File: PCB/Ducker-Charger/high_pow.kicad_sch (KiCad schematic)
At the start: 37 parts, among them Q1 NCE3080K, Q2 NCE3080K, Q3 NCE3080K, Q4 NCE3080K, Q5 NCE3080K, U1 BQ25713RSNR, U2 TPS25750DRJKR

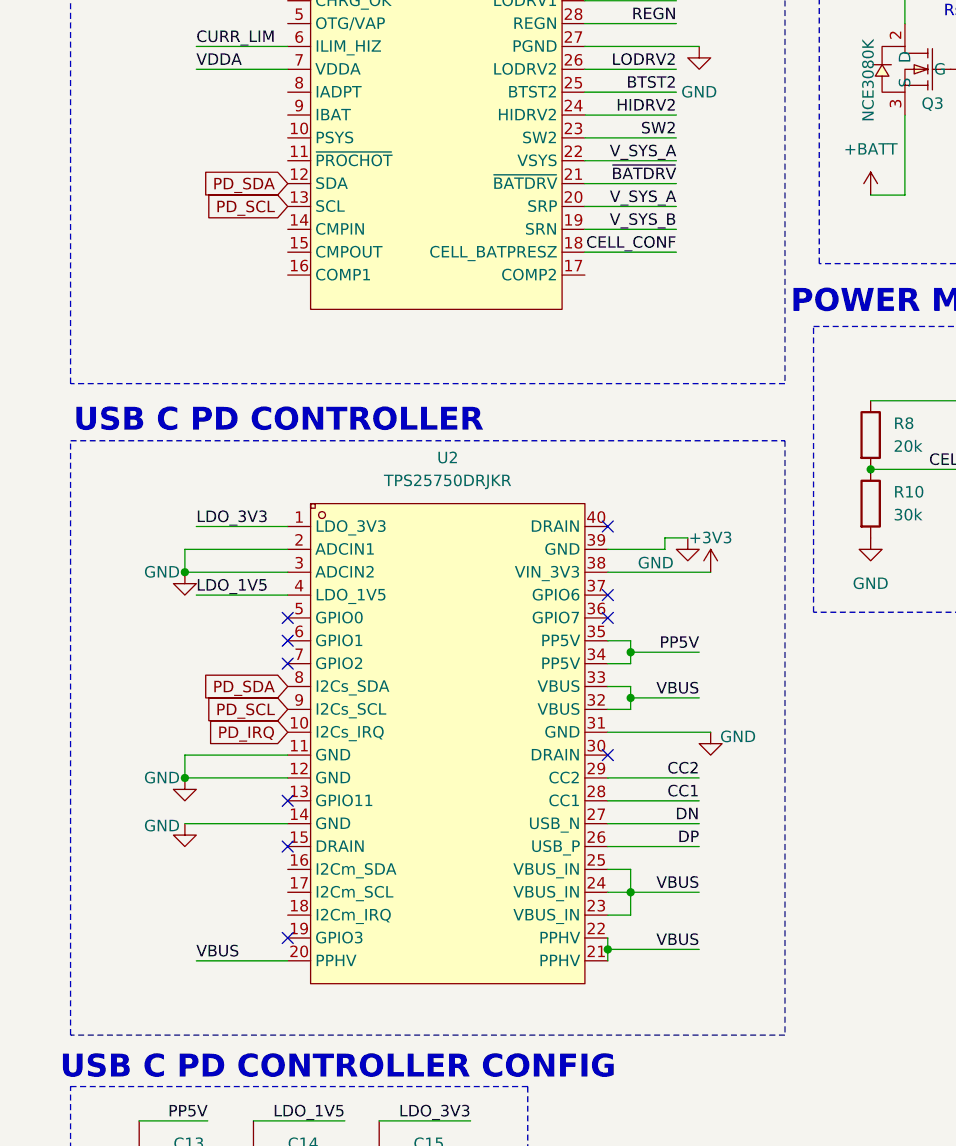
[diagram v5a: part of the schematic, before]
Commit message: fix: I2C is now a BUS, no longer a global label
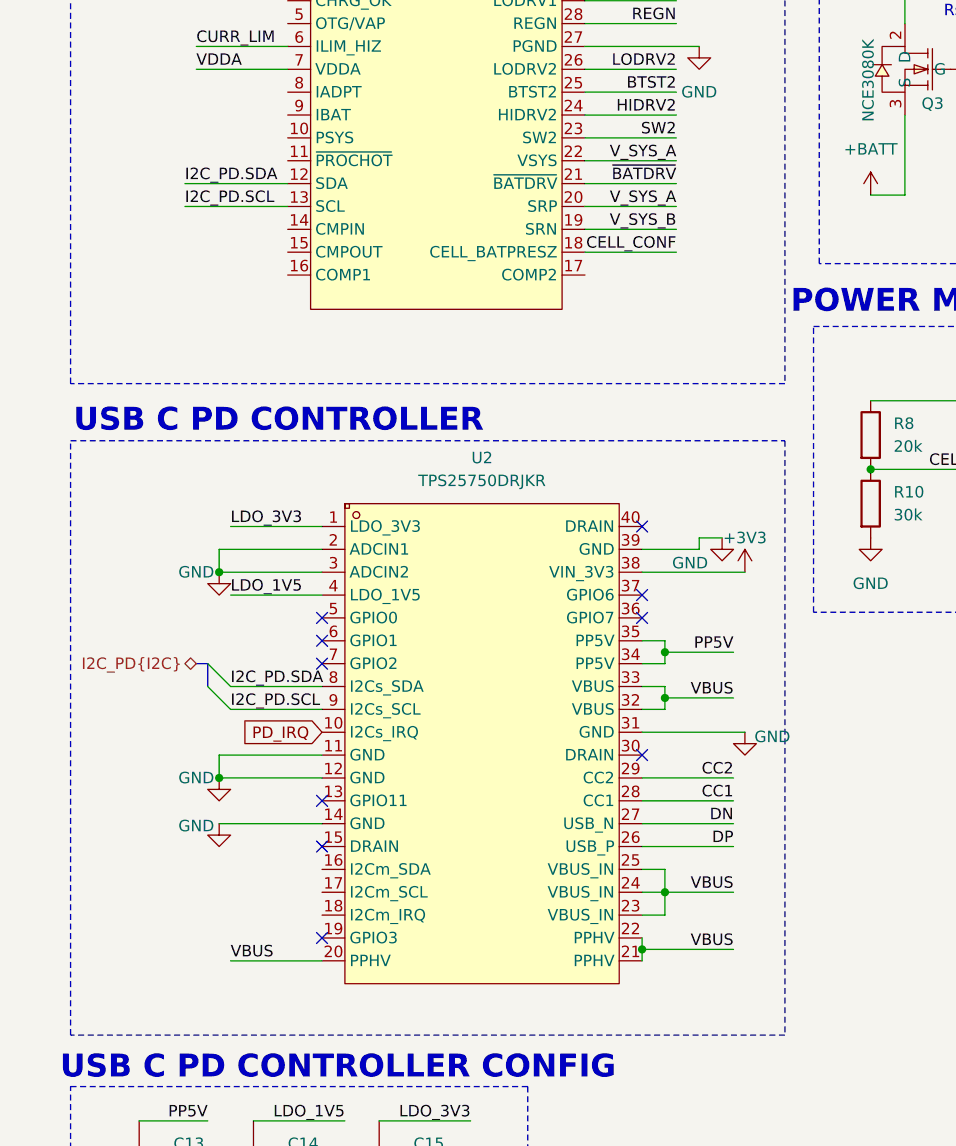
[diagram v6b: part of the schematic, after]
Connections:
- net PD_SCL renamed I2C_PD.SCL
- net PD_SDA renamed I2C_PD.SDA
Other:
- moved on the sheet: U2

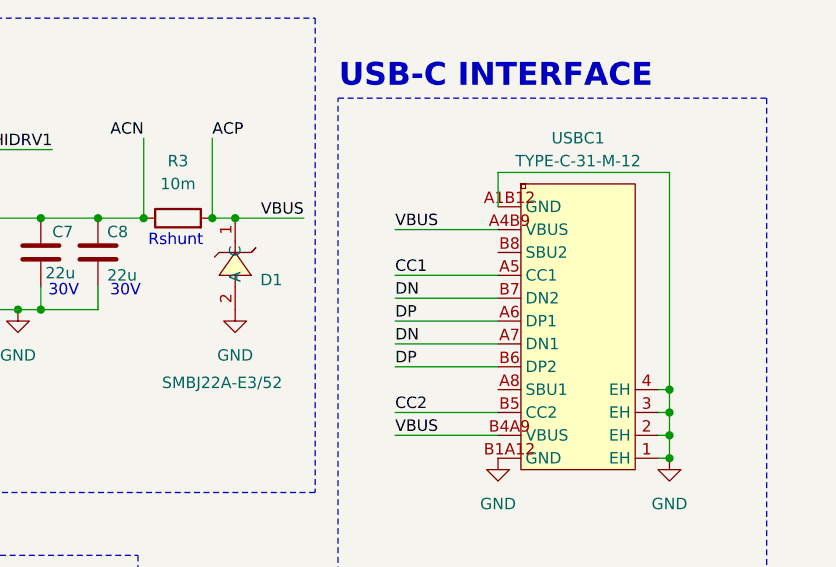
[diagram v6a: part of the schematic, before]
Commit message: fix: replaced Schottky Diode sym
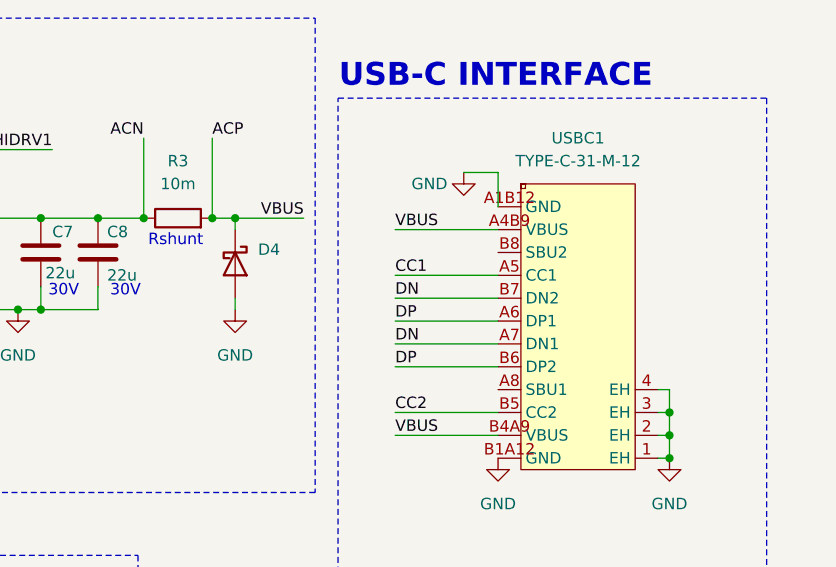
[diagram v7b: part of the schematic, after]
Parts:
- removed D1: SMBJ22A-E3/52, EasyEDA:SMB_L4.3-W3.6-LS5.4-RD, symbol EasyEDA:SMBJ22A-E3_52
- added D4: SMBJ22A-E3/52, EasyEDA:SMB_L4.3-W3.6-LS5.4-RD, symbol Device:D_Schottky
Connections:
- net ACP: now also D4.1 (K)
- net GND: now also D4.2 (A)
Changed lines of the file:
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@@
 	)
 	(junction
-		(at 270.51 71.12)
-		(diameter 0)
-		(color 0 0 0 0)
-	)
-	(junction
 		(at 270.51 76.2)
 		(diameter 0)
@@
 	)
 	(junction
-		(at 222.25 52.07)
-		(diameter 0)
-		(color 0 0 0 0)
-	)
-	(junction
 		(at 193.04 52.07)
 		(diameter 0)
@@
 	)
 	(junction
-		(at 130.81 105.41)
+		(at 270.51 78.74)
 		(diameter 0)
 		(color 0 0 0 0)
 	)
 	(junction
-		(at 109.22 52.07)
+		(at 130.81 105.41)
 		(diameter 0)
 		(color 0 0 0 0)
 	)
 	(junction
-		(at 270.51 78.74)
+		(at 109.22 52.07)
 		(diameter 0)
 		(color 0 0 0 0)
@@
 	)
 	(junction
+		(at 222.25 52.07)
+		(diameter 0)
+		(color 0 0 0 0)
+	)
+	(junction
 		(at 124.46 52.07)
 		(diameter 0)
@@
 	(wire
 		(pts
+			(xy 222.25 53.34) (xy 222.25 52.07)
+		)
+		(stroke
+			(width 0)
+			(type default)
+		)
+	)
+	(wire
+		(pts
 			(xy 80.01 149.86) (xy 82.55 149.86)
 		)
@@
 	(wire
 		(pts
-			(xy 251.46 46.99) (xy 251.46 50.8)
-		)
-		(stroke
-			(width 0)
-			(type default)
-		)
-	)
-	(wire
-		(pts
 			(xy 109.22 74.93) (xy 105.41 74.93)
 		)
@@
 	(wire
 		(pts
+			(xy 251.46 46.99) (xy 251.46 50.8)
+		)
+		(stroke
+			(width 0)
+			(type default)
+		)
+	)
+	(wire
+		(pts
+			(xy 247.65 46.99) (xy 251.46 46.99)
+		)
+		(stroke
+			(width 0)
+			(type default)
+		)
+	)
+	(wire
+		(pts
 			(xy 269.24 71.12) (xy 270.51 71.12)
 		)
@@
 	(wire
 		(pts
+			(xy 222.25 52.07) (xy 229.87 52.07)
+		)
+		(stroke
+			(width 0)
+			(type default)
+		)
+	)
+	(wire
+		(pts
 			(xy 90.17 125.73) (xy 82.55 125.73)
 		)
@@
 	(wire
 		(pts
-			(xy 82.55 130.81) (xy 90.17 130.81)
+			(xy 222.25 60.96) (xy 222.25 62.23)
 		)
 		(stroke
@@
 	(wire
 		(pts
-			(xy 34.29 132.08) (xy 44.45 132.08)
+			(xy 82.55 130.81) (xy 90.17 130.81)
 		)
 		(stroke
@@
 	(wire
 		(pts
-			(xy 138.43 59.69) (xy 138.43 62.23)
+			(xy 34.29 132.08) (xy 44.45 132.08)
 		)
 		(stroke
@@
 	(wire
 		(pts
-			(xy 240.03 53.34) (xy 251.46 53.34)
+			(xy 138.43 59.69) (xy 138.43 62.23)
 		)
 		(stroke
@@
 	(wire
 		(pts
-			(xy 116.84 66.04) (xy 116.84 60.96)
+			(xy 240.03 53.34) (xy 251.46 53.34)
 		)
 		(stroke
@@
 	(wire
 		(pts
-			(xy 222.25 52.07) (xy 229.87 52.07)
+			(xy 116.84 66.04) (xy 116.84 60.96)
 		)
 		(stroke
@@
 	(wire
 		(pts
-			(xy 33.02 137.16) (xy 44.45 137.16)
+			(xy 219.71 52.07) (xy 222.25 52.07)
 		)
 		(stroke
@@
 	(wire
 		(pts
-			(xy 80.01 129.54) (xy 82.55 129.54)
+			(xy 33.02 137.16) (xy 44.45 137.16)
 		)
 		(stroke
@@
 	(wire
 		(pts
-			(xy 270.51 71.12) (xy 270.51 46.99)
+			(xy 80.01 129.54) (xy 82.55 129.54)
 		)
 		(stroke
@@
 	(wire
 		(pts
-			(xy 219.71 52.07) (xy 222.25 52.07)
-		)
-		(stroke
-			(width 0)
-			(type default)
-		)
-	)
-	(wire
-		(pts
 			(xy 132.08 62.23) (xy 129.54 62.23)
 		)
@@
 	(wire
 		(pts
-			(xy 270.51 46.99) (xy 251.46 46.99)
-		)
-		(stroke
-			(width 0)
-			(type default)
-		)
-	)
-	(wire
-		(pts
 			(xy 168.91 60.96) (xy 168.91 59.69)
 		)
@@
 	)
 	(symbol
+		(lib_id "power:GND")
+		(at 247.65 46.99 0)
+		(unit 1)
+		(exclude_from_sim no)
+		(in_bom yes)
+		(on_board yes)
+		(dnp no)
+		(property "Reference" "#PWR0124"
+			(at 247.65 53.34 0)
+			(effects
+				(font
+					(size 1.27 1.27)
+				)
+				(hide yes)
+			)
+		)
+		(property "Value" "GND"
+			(at 243.84 48.26 0)
+			(effects
+				(font
+					(size 1.27 1.27)
+				)
+			)
+		)
+		(property "Footprint" ""
+			(at 247.65 46.99 0)
+			(effects
+				(font
+					(size 1.27 1.27)
+				)
+				(hide yes)
+			)
+		)
+		(property "Datasheet" ""
+			(at 247.65 46.99 0)
+			(effects
+				(font
+					(size 1.27 1.27)
+				)
+				(hide yes)
+			)
+		)
+		(property "Description" "Power symbol creates a global label with name \"GND\" , ground"
+			(at 247.65 46.99 0)
+			(effects
+				(font
+					(size 1.27 1.27)
+				)
+				(hide yes)
+			)
+		)
+		(pin "1"
+		)
+		(instances
+			(project "Ducker-Charger"
+				(path "/74790d6c-a68e-4e6d-b4a9-43de1843f817/ccd240c6-b24b-451e-a22e-a82e757ea5cc"
+					(reference "#PWR0124")
+					(unit 1)
+				)
+			)
+		)
+	)
+	(symbol
 		(lib_id "Device:L")
 		(at 165.1 52.07 90)
@@
 	)
 	(symbol
-		(lib_id "EasyEDA:SMBJ22A-E3_52")
-		(at 220.98 58.42 270)
-		(unit 1)
-		(exclude_from_sim no)
-		(in_bom yes)
-		(on_board yes)
-		(dnp no)
-		(property "Reference" "D1"
-			(at 225.044 58.928 90)
-			(effects
-				(font
-					(size 1.27 1.27)
-				)
-				(justify left)
-			)
-		)
-		(property "Value" "SMBJ22A-E3/52"
-			(at 214.122 70.358 90)
-			(effects
-				(font
-					(size 1.27 1.27)
-				)
-				(justify left)
-			)
-		)
-		(property "Footprint" "EasyEDA:SMB_L4.3-W3.6-LS5.4-RD"
-			(at 214.63 58.42 0)
-			(effects
-				(font
-					(size 1.27 1.27)
-				)
-				(hide yes)
-			)
-		)
-		(property "Datasheet" ""
-			(at 220.98 58.42 0)
-			(effects
-				(font
-					(size 1.27 1.27)
-				)
-				(hide yes)
-			)
-		)
-		(property "Description" ""
-			(at 220.98 58.42 0)
-			(effects
-				(font
-					(size 1.27 1.27)
-				)
-				(hide yes)
-			)
-		)
-		(property "LCSC Part" "C3698580"
-			(at 212.09 58.42 0)
-			(effects
-				(font
-					(size 1.27 1.27)
-				)
-				(hide yes)
-			)
-		)
-		(pin "2"
-		)
-		(pin "1"
-		)
-		(instances
-			(project ""
-				(path "/74790d6c-a68e-4e6d-b4a9-43de1843f817/ccd240c6-b24b-451e-a22e-a82e757ea5cc"
-					(reference "D1")
-					(unit 1)
-				)
-			)
-		)
-	)
-	(symbol
 		(lib_id "Device:C")
 		(at 50.8 181.61 0)
@@
 					(unit 1)
 				)
+			)
+		)
+	)
+	(symbol
+		(lib_id "Device:D_Schottky")
+		(at 222.25 57.15 270)
+		(unit 1)
+		(exclude_from_sim no)
+		(in_bom yes)
+		(on_board yes)
+		(dnp no)
+		(property "Reference" "D4"
+			(at 224.79 55.5624 90)
+			(effects
+				(font
+					(size 1.27 1.27)
+				)
+				(justify left)
+			)
+		)
+		(property "Value" "SMBJ22A-E3/52"
+			(at 227.584 57.658 90)
+			(effects
+				(font
+					(size 1.27 1.27)
+				)
+				(justify left)
+				(hide yes)
+			)
+		)
+		(property "Footprint" "EasyEDA:SMB_L4.3-W3.6-LS5.4-RD"
+			(at 222.25 57.15 0)
+			(effects
+				(font
+					(size 1.27 1.27)
+				)
+				(hide yes)
+			)
+		)
+		(property "Datasheet" "~"
+			(at 222.25 57.15 0)
+			(effects
+				(font
+					(size 1.27 1.27)
+				)
+				(hide yes)
+			)
+		)
+		(property "Description" "Schottky diode"
+			(at 222.25 57.15 0)
+			(effects
+				(font
+					(size 1.27 1.27)
+				)
+				(hide yes)
+			)
+		)
+		(pin "1"
+		)
+		(pin "2"
+		)
+		(instances
+			(project ""
+				(path "/74790d6c-a68e-4e6d-b4a9-43de1843f817/ccd240c6-b24b-451e-a22e-a82e757ea5cc"
+					(reference "D4")
+					(unit 1)
+				)

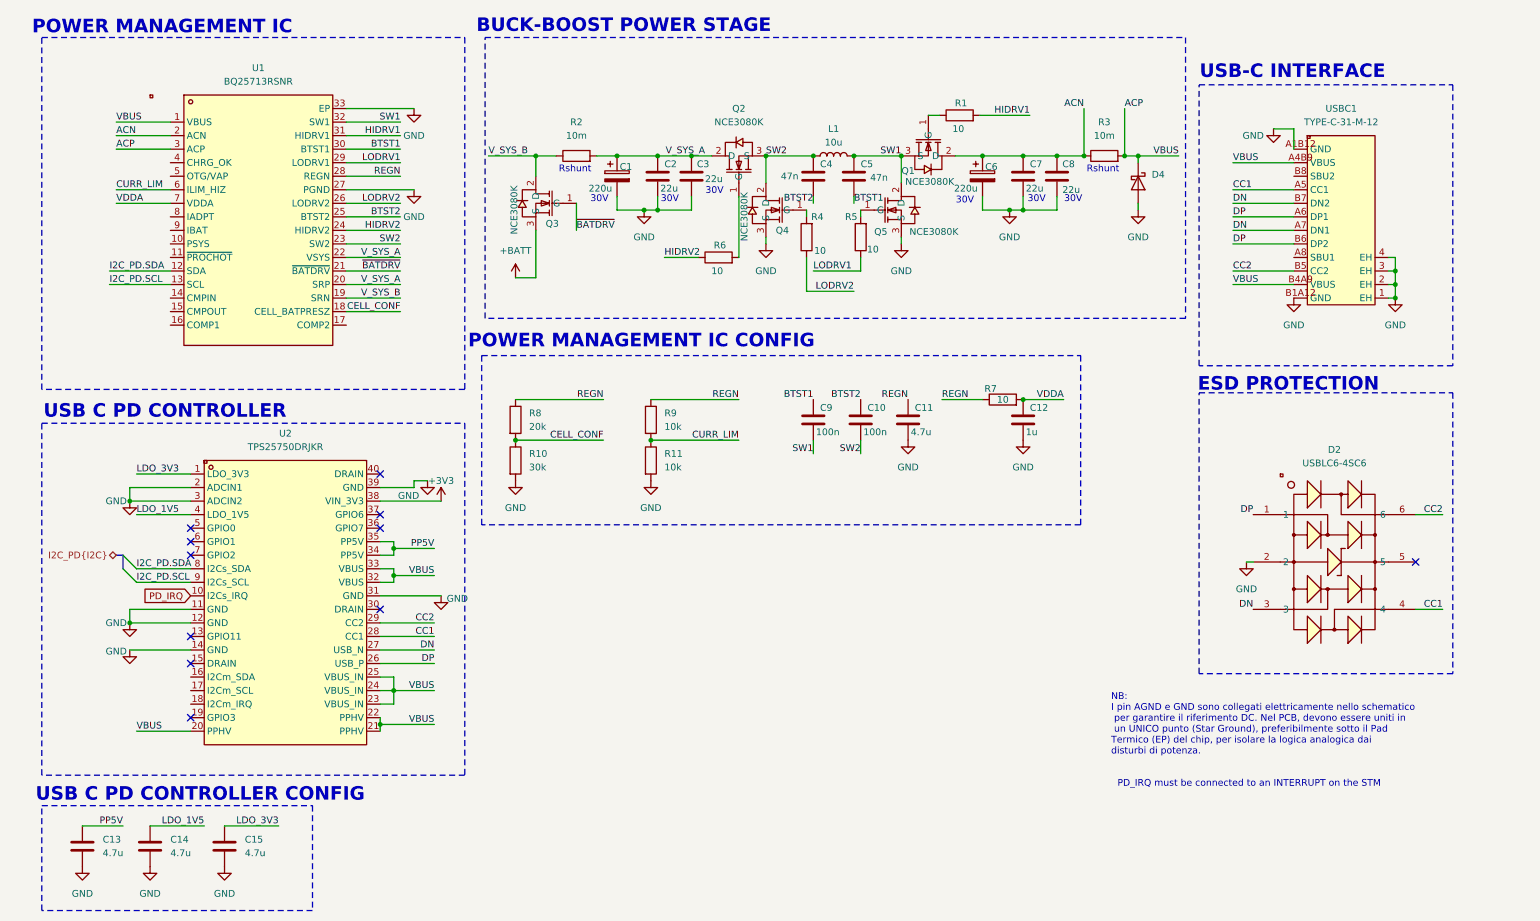
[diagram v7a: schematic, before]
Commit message: fix: readability of Buck-Boost power stage
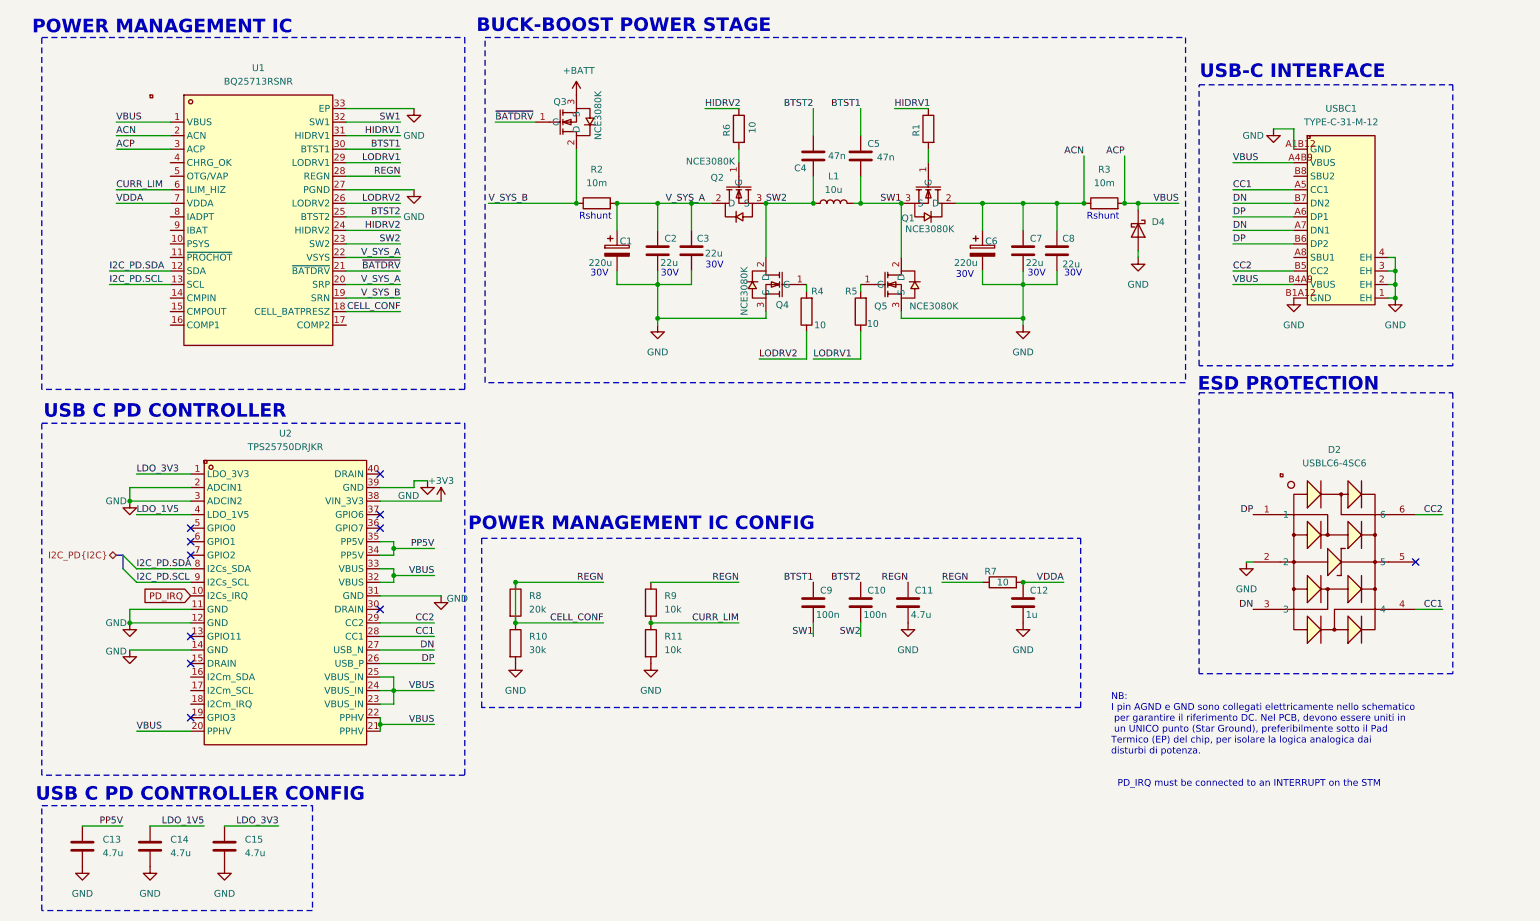
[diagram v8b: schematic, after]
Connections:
- net REGN is gone; now on net CELL_CONF: C11.1, R7.1, R8.1, R9.1, U1.28 (REGN)
- net BTST1: now also C5.1; no longer C5.2
- net HIDRV1: now also R1.1; no longer R1.2
- net SW1: now also C5.2; no longer C5.1
- net at Q1.1 (G): now also R1.2; no longer R1.1
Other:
- moved on the sheet: C1, C10, C11, C12, C2, C3, C4, C5, C6, C7, C8, C9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
